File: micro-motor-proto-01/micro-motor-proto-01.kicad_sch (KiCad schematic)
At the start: 2 parts, among them J1 PhA, J2 PhB

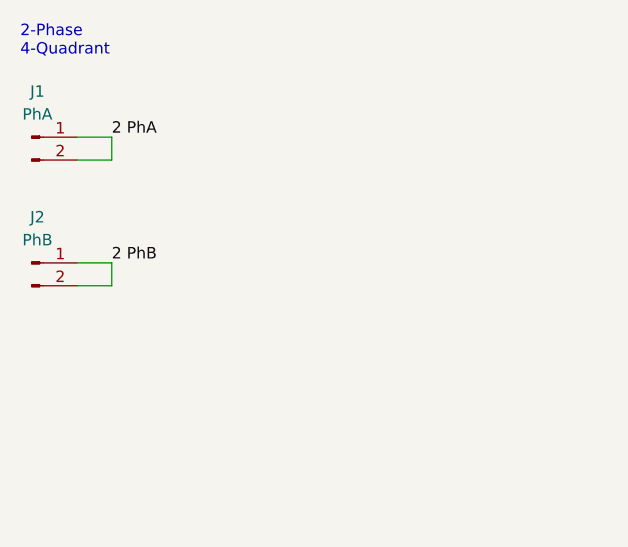
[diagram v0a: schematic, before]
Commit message: Simplified to get nets right for early dev.
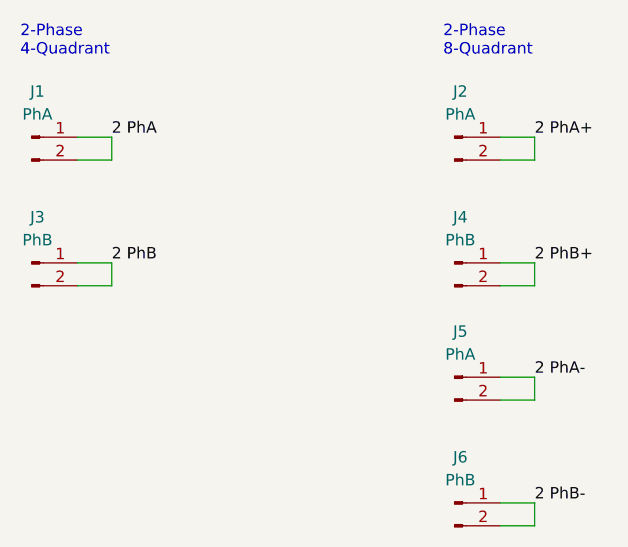
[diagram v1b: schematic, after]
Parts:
- added J2, J5: PhA, Connector_PinHeader_2.54mm:PinHeader_1x02_P2.54mm_Vertical, symbol Connector:Conn_01x02_Male
- added J4, J6: PhB, Connector_PinHeader_2.54mm:PinHeader_1x02_P2.54mm_Vertical, symbol Connector:Conn_01x02_Male
- renumbered J2 to J3
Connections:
- new net 2 PhA+: J2.1 (Pin_1), J2.2 (Pin_2)
- new net 2 PhA-: J5.1 (Pin_1), J5.2 (Pin_2)
- new net 2 PhB+: J4.1 (Pin_1), J4.2 (Pin_2)
- new net 2 PhB-: J6.1 (Pin_1), J6.2 (Pin_2)
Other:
- note added: "2-Phase 8-Quadrant"
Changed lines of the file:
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@@
 (kicad_sch (version 20211123) (generator eeschema)
   (paper "A4")
+  (wire (pts (xy 102.87 52.07) (xy 99.06 52.07))
+    (stroke (width 0) (type default) (color 0 0 0 0))
+  )
   (wire (pts (xy 52.07 63.5) (xy 55.88 63.5))
     (stroke (width 0) (type default) (color 0 0 0 0))
   )
+  (wire (pts (xy 99.06 76.2) (xy 102.87 76.2))
+    (stroke (width 0) (type default) (color 0 0 0 0))
+  )
+  (wire (pts (xy 102.87 63.5) (xy 102.87 66.04))
+    (stroke (width 0) (type default) (color 0 0 0 0))
+  )
   (wire (pts (xy 55.88 49.53) (xy 55.88 52.07))
+    (stroke (width 0) (type default) (color 0 0 0 0))
+  )
+  (wire (pts (xy 102.87 49.53) (xy 102.87 52.07))
+    (stroke (width 0) (type default) (color 0 0 0 0))
+  )
+  (wire (pts (xy 102.87 78.74) (xy 99.06 78.74))
+    (stroke (width 0) (type default) (color 0 0 0 0))
+  )
+  (wire (pts (xy 102.87 76.2) (xy 102.87 78.74))
     (stroke (width 0) (type default) (color 0 0 0 0))
   )
@@
     (stroke (width 0) (type default) (color 0 0 0 0))
   )
+  (wire (pts (xy 99.06 63.5) (xy 102.87 63.5))
+    (stroke (width 0) (type default) (color 0 0 0 0))
+  )
+  (wire (pts (xy 102.87 90.17) (xy 102.87 92.71))
+    (stroke (width 0) (type default) (color 0 0 0 0))
+  )
+  (wire (pts (xy 102.87 66.04) (xy 99.06 66.04))
+    (stroke (width 0) (type default) (color 0 0 0 0))
+  )
+  (wire (pts (xy 99.06 49.53) (xy 102.87 49.53))
+    (stroke (width 0) (type default) (color 0 0 0 0))
+  )
+  (wire (pts (xy 102.87 92.71) (xy 99.06 92.71))
+    (stroke (width 0) (type default) (color 0 0 0 0))
+  )
   (wire (pts (xy 55.88 52.07) (xy 52.07 52.07))
+    (stroke (width 0) (type default) (color 0 0 0 0))
+  )
+  (wire (pts (xy 99.06 90.17) (xy 102.87 90.17))
     (stroke (width 0) (type default) (color 0 0 0 0))
   )
@@
     (stroke (width 0) (type default) (color 0 0 0 0))
   )
+  (text "2-Phase\n8-Quadrant" (at 92.71 40.64 0)
+    (effects (font (size 1.27 1.27)) (justify left bottom))
+  )
   (text "2-Phase\n4-Quadrant" (at 45.72 40.64 0)
+    (effects (font (size 1.27 1.27)) (justify left bottom))
+  )
+  (label "2 PhA+" (at 102.87 49.53 0)
+    (effects (font (size 1.27 1.27)) (justify left bottom))
+  )
+  (label "2 PhB-" (at 102.87 90.17 0)
+    (effects (font (size 1.27 1.27)) (justify left bottom))
+  )
+  (label "2 PhB+" (at 102.87 63.5 0)
     (effects (font (size 1.27 1.27)) (justify left bottom))
   )
@@
     (effects (font (size 1.27 1.27)) (justify left bottom))
   )
+  (label "2 PhA-" (at 102.87 76.2 0)
+    (effects (font (size 1.27 1.27)) (justify left bottom))
+  )
+  (symbol (lib_id "Connector:Conn_01x02_Male") (at 93.98 49.53 0) (unit 1)
+    (in_bom yes) (on_board yes) (fields_autoplaced)
+    (property "Reference" "J2" (id 0) (at 94.615 44.45 0))
+    (property "Value" "PhA" (id 1) (at 94.615 46.99 0))
+    (property "Footprint" "Connector_PinHeader_2.54mm:PinHeader_1x02_P2.54mm_Vertical" (id 2) (at 93.98 49.53 0)
+      (effects (font (size 1.27 1.27)) hide)
+    )
+    (property "Datasheet" "~" (id 3) (at 93.98 49.53 0)
+      (effects (font (size 1.27 1.27)) hide)
+    )
+    (pin "1")
+    (pin "2")
+  )
+  (symbol (lib_id "Connector:Conn_01x02_Male") (at 93.98 90.17 0) (unit 1)
+    (in_bom yes) (on_board yes) (fields_autoplaced)
+    (property "Reference" "J6" (id 0) (at 94.615 85.09 0))
+    (property "Value" "PhB" (id 1) (at 94.615 87.63 0))
+    (property "Footprint" "Connector_PinHeader_2.54mm:PinHeader_1x02_P2.54mm_Vertical" (id 2) (at 93.98 90.17 0)
+      (effects (font (size 1.27 1.27)) hide)
+    )
+    (property "Datasheet" "~" (id 3) (at 93.98 90.17 0)
+      (effects (font (size 1.27 1.27)) hide)
+    )
+    (pin "1")
+    (pin "2")
+  )
   (symbol (lib_id "Connector:Conn_01x02_Male") (at 46.99 63.5 0) (unit 1)
     (in_bom yes) (on_board yes) (fields_autoplaced)
-    (property "Reference" "J2" (id 0) (at 47.625 58.42 0))
+    (property "Reference" "J3" (id 0) (at 47.625 58.42 0))
     (property "Value" "PhB" (id 1) (at 47.625 60.96 0))
     (property "Footprint" "Connector_PinHeader_2.54mm:PinHeader_1x02_P2.54mm_Vertical" (id 2) (at 46.99 63.5 0)
@@
     )
     (property "Datasheet" "~" (id 3) (at 46.99 63.5 0)
+      (effects (font (size 1.27 1.27)) hide)
+    )
+    (pin "1")
+    (pin "2")
+  )
+  (symbol (lib_id "Connector:Conn_01x02_Male") (at 93.98 63.5 0) (unit 1)
+    (in_bom yes) (on_board yes) (fields_autoplaced)
+    (property "Reference" "J4" (id 0) (at 94.615 58.42 0))
+    (property "Value" "PhB" (id 1) (at 94.615 60.96 0))
+    (property "Footprint" "Connector_PinHeader_2.54mm:PinHeader_1x02_P2.54mm_Vertical" (id 2) (at 93.98 63.5 0)
+      (effects (font (size 1.27 1.27)) hide)
+    )
+    (property "Datasheet" "~" (id 3) (at 93.98 63.5 0)
+      (effects (font (size 1.27 1.27)) hide)
+    )
+    (pin "1")
+    (pin "2")
+  )
+  (symbol (lib_id "Connector:Conn_01x02_Male") (at 93.98 76.2 0) (unit 1)
+    (in_bom yes) (on_board yes) (fields_autoplaced)
+    (property "Reference" "J5" (id 0) (at 94.615 71.12 0))
+    (property "Value" "PhA" (id 1) (at 94.615 73.66 0))
+    (property "Footprint" "Connector_PinHeader_2.54mm:PinHeader_1x02_P2.54mm_Vertical" (id 2) (at 93.98 76.2 0)
+      (effects (font (size 1.27 1.27)) hide)
+    )
+    (property "Datasheet" "~" (id 3) (at 93.98 76.2 0)
       (effects (font (size 1.27 1.27)) hide)
     )
@@
       (reference "J1") (unit 1) (value "PhA") (footprint "Connector_PinHeader_2.54mm:PinHeader_1x02_P2.54mm_Vertical")
     )
+    (path "/1ebdb82e-d3ba-445a-832c-d81afdf5950c"
+      (reference "J2") (unit 1) (value "PhA") (footprint "Connector_PinHeader_2.54mm:PinHeader_1x02_P2.54mm_Vertical")
+    )
     (path "/99ce1eed-3a39-4a28-ab92-dee4906f234c"
-      (reference "J2") (unit 1) (value "PhB") (footprint "Connector_PinHeader_2.54mm:PinHeader_1x02_P2.54mm_Vertical")
+      (reference "J3") (unit 1) (value "PhB") (footprint "Connector_PinHeader_2.54mm:PinHeader_1x02_P2.54mm_Vertical")
+    )
+    (path "/bbafaff6-5ec7-4e49-9471-02b67816950c"
+      (reference "J4") (unit 1) (value "PhB") (footprint "Connector_PinHeader_2.54mm:PinHeader_1x02_P2.54mm_Vertical")
+    )
+    (path "/d2026d41-340c-477b-820f-ba8d3da88151"
+      (reference "J5") (unit 1) (value "PhA") (footprint "Connector_PinHeader_2.54mm:PinHeader_1x02_P2.54mm_Vertical")
+    )
+    (path "/58c6a8ea-a254-44ac-a2f4-67ba9aad0c5d"
+      (reference "J6") (unit 1) (value "PhB") (footprint "Connector_PinHeader_2.54mm:PinHeader_1x02_P2.54mm_Vertical")
     )
   )

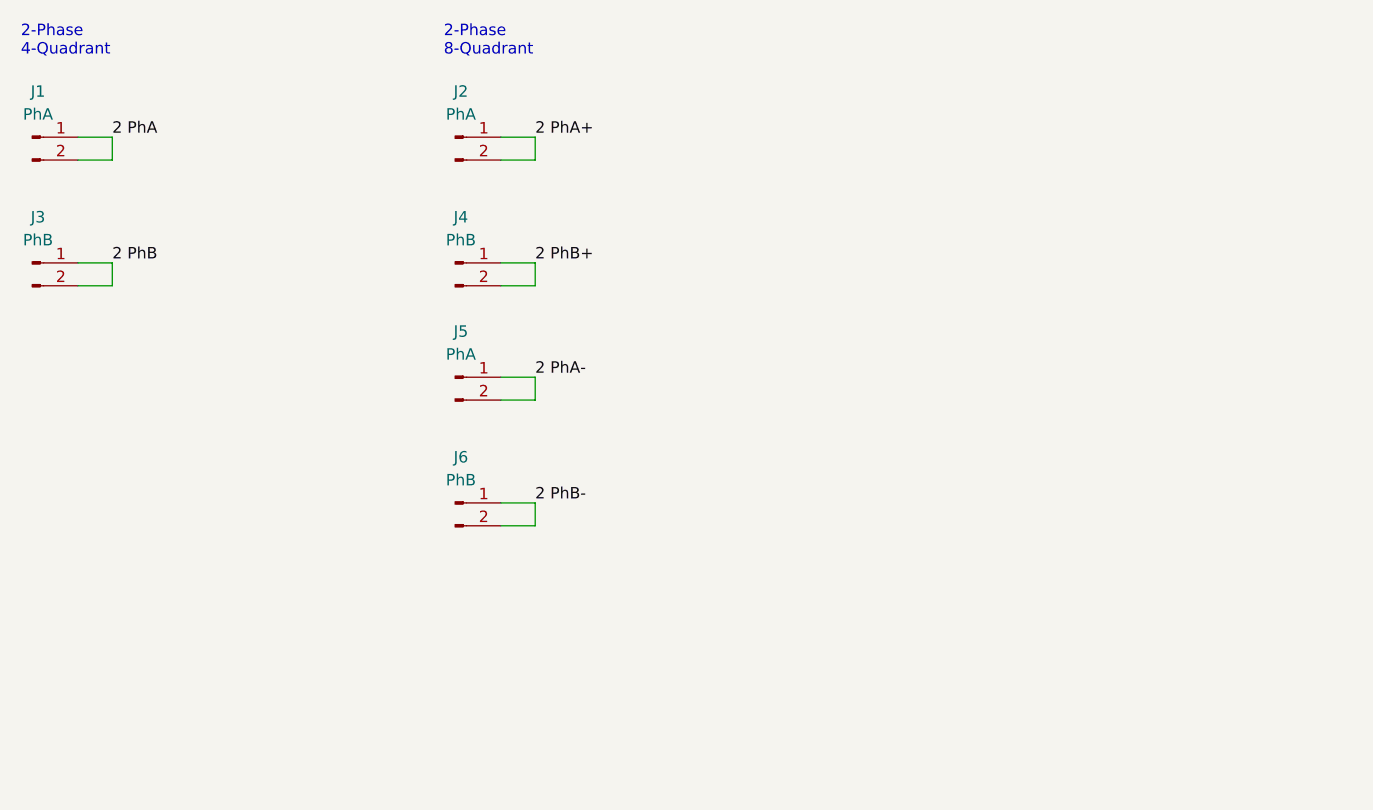
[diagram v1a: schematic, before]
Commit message: Schematic & layout updates
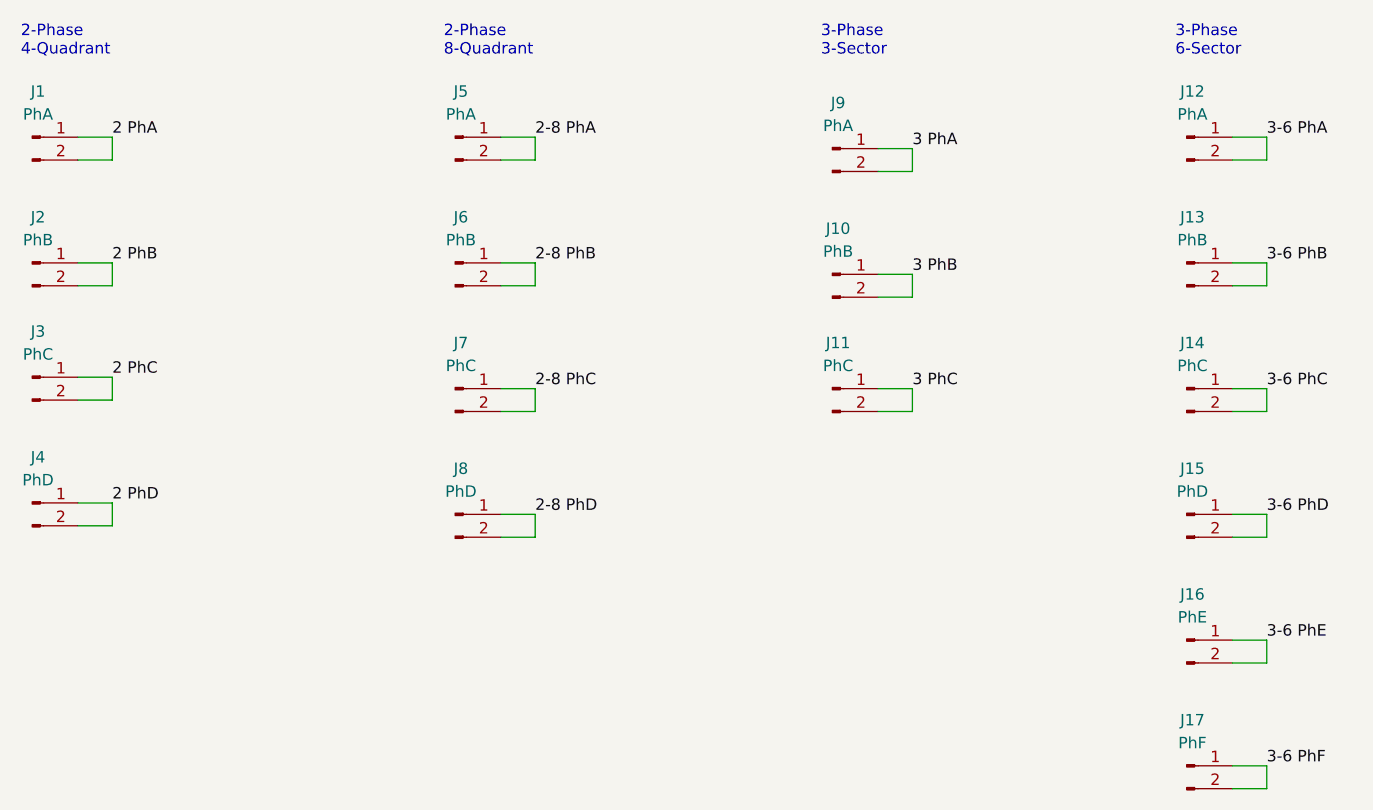
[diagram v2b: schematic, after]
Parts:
- added J11, J14, J3, J7: PhC, Connector_PinHeader_2.54mm:PinHeader_1x02_P2.54mm_Vertical, symbol Connector:Conn_01x02_Male
- added J12: PhA, Connector_PinHeader_2.54mm:PinHeader_1x02_P2.54mm_Vertical, symbol Connector:Conn_01x02_Male
- added J13: PhB, Connector_PinHeader_2.54mm:PinHeader_1x02_P2.54mm_Vertical, symbol Connector:Conn_01x02_Male
- added J15, J4, J8: PhD, Connector_PinHeader_2.54mm:PinHeader_1x02_P2.54mm_Vertical, symbol Connector:Conn_01x02_Male
- added J16: PhE, Connector_PinHeader_2.54mm:PinHeader_1x02_P2.54mm_Vertical, symbol Connector:Conn_01x02_Male
- added J17: PhF, Connector_PinHeader_2.54mm:PinHeader_1x02_P2.54mm_Vertical, symbol Connector:Conn_01x02_Male
- renumbered J6 to J10, J3 to J2, J2 to J5, J4 to J6, J5 to J9
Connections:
- net 2 PhA+ renamed 2-8 PhA
- net 2 PhA- renamed 3 PhA
- net 2 PhB+ renamed 2-8 PhB
- net 2 PhB- renamed 3 PhB
- new net 2 PhC: J3.1 (Pin_1), J3.2 (Pin_2)
- new net 2 PhD: J4.1 (Pin_1), J4.2 (Pin_2)
- new net 2-8 PhC: J7.1 (Pin_1), J7.2 (Pin_2)
- new net 2-8 PhD: J8.1 (Pin_1), J8.2 (Pin_2)
- new net 3 PhC: J11.1 (Pin_1), J11.2 (Pin_2)
- new net 3-6 PhA: J12.1 (Pin_1), J12.2 (Pin_2)
- new net 3-6 PhB: J13.1 (Pin_1), J13.2 (Pin_2)
- new net 3-6 PhC: J14.1 (Pin_1), J14.2 (Pin_2)
- new net 3-6 PhD: J15.1 (Pin_1), J15.2 (Pin_2)
- new net 3-6 PhE: J16.1 (Pin_1), J16.2 (Pin_2)
- new net 3-6 PhF: J17.1 (Pin_1), J17.2 (Pin_2)
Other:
- note added: "3-Phase 3-Sector"
- note added: "3-Phase 6-Sector"
- moved on the sheet: J10, J9
